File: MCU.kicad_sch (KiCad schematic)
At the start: 21 parts, among them J1 DEBUG, Q1 BC817, Q2 BC817, SW1 RST, U6 ESP32-S3-WROOM-1

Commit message: -add some changes to power section and display
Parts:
- removed J1: DEBUG, Connector_PinHeader_2.54mm:PinHeader_2x06_P2.54mm_Vertical_SMD, symbol Connector_Generic:Conn_02x06_Odd_Even
- removed TP2: P0.29, TestPoint:TestPoint_Pad_D2.0mm, symbol Connector:TestPoint
- added J10: DEBUG, Connector_PinHeader_2.54mm:PinHeader_2x05_P2.54mm_Vertical_SMD, symbol Connector_Generic:Conn_02x05_Odd_Even
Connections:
- net +3.3V: now also J10.2 (Pin_2)
- net DTR: now also J10.9 (Pin_9)
- net GND: now also J10.10 (Pin_10)
- net GPIO_0: now also J10.3 (Pin_3)
- net GPIO_12/JTAG_TDI: now also J10.6 (Pin_6)
- net GPIO_13/JTAG_TCK: now also J10.4 (Pin_4)
- net GPIO_2: now also U6.21 (GPIO13/TOUCH13/ADC2_CH2/FSPIQ/FSPIIO7/SUBSPIQ); no longer U6.38 (GPIO2/TOUCH2/ADC1_CH1)
- net GPIO_25: now also U6.5 (GPIO5/TOUCH5/ADC1_CH4); no longer U6.21 (GPIO13/TOUCH13/ADC2_CH2/FSPIQ/FSPIIO7/SUBSPIQ)
- net GPIO_32: now also U6.39 (GPIO1/TOUCH1/ADC1_CH0); no longer U6.11 (GPIO18/U1RXD/ADC2_CH7/CLK_OUT3)
- net GPIO_33: now also U6.38 (GPIO2/TOUCH2/ADC1_CH1); no longer U6.23 (GPIO21)
- net GPIO_34: now also U6.26 (GPIO45); no longer U6.31 (GPIO38/FSPIWP/SUBSPIWP)
- net GPIO_35: now also U6.16 (GPIO46); no longer U6.26 (GPIO45)
- net GPIO_4: now also U6.11 (GPIO18/U1RXD/ADC2_CH7/CLK_OUT3); no longer U6.4 (GPIO4/TOUCH4/ADC1_CH3)
- net GPIO_5: now also U6.23 (GPIO21); no longer U6.5 (GPIO5/TOUCH5/ADC1_CH4)
- net I2S_DOUT: now also U6.4 (GPIO4/TOUCH4/ADC1_CH3); no longer U6.8 (GPIO15/U0RTS/ADC2_CH4/XTAL_32K_P)
- net RESET: now also J10.1 (Pin_1)
- net RTS: now also J10.8 (Pin_8)
- net SD_SPI_CS: now also U6.31 (GPIO38/FSPIWP/SUBSPIWP); no longer U6.16 (GPIO46)
- net I2C_SCL: now reaches U1.7 (P0.29)
- net I2C_SCL: now also U6.9 (GPIO16/U0CTS/ADC2_CH5/XTAL_32K_N)
- net GPIO_44/RXD0: now reaches U6.36 (U0RXD/GPIO44/CLK_OUT2)
- net GPIO_44/RXD0: now also U1.41 (P0.12), J10.7 (Pin_7)
- net GPIO_43/TXD0: now reaches U6.37 (U0TXD/GPIO43/CLK_OUT1)
- net GPIO_43/TXD0: now also U1.39 (P1.10), J10.5 (Pin_5)
- net I2C_SDA: now reaches U1.23 (P0.01)
- net I2C_SDA: now also U6.8 (GPIO15/U0RTS/ADC2_CH4/XTAL_32K_P)
- removed net GPIO_1/TXD0: U1.41 (P0.12), U6.39 (GPIO1/TOUCH1/ADC1_CH0)
- net GPIO_3/RXD0: no longer names the net of U6.15 (GPIO3/TOUCH3/ADC1_CH2)
- net GPIO_3/RXD0: no longer U1.39 (P1.10)
- no-connect marks 6 -> 3
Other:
- moved on the sheet: C13, C14, FB8, R31, R32, U1

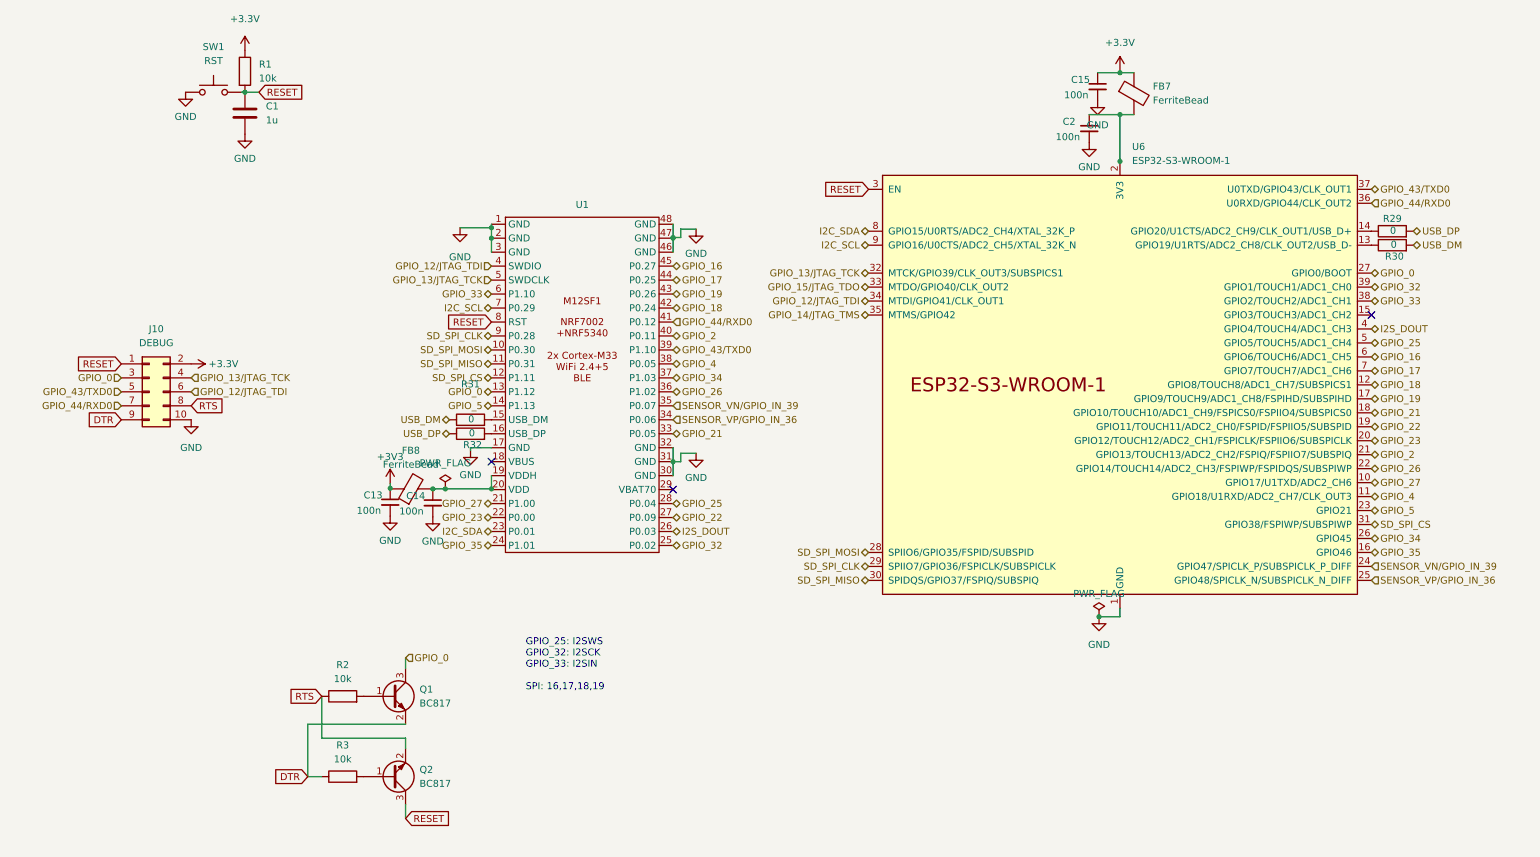
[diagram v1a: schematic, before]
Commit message: -enh repin mcu in schematic
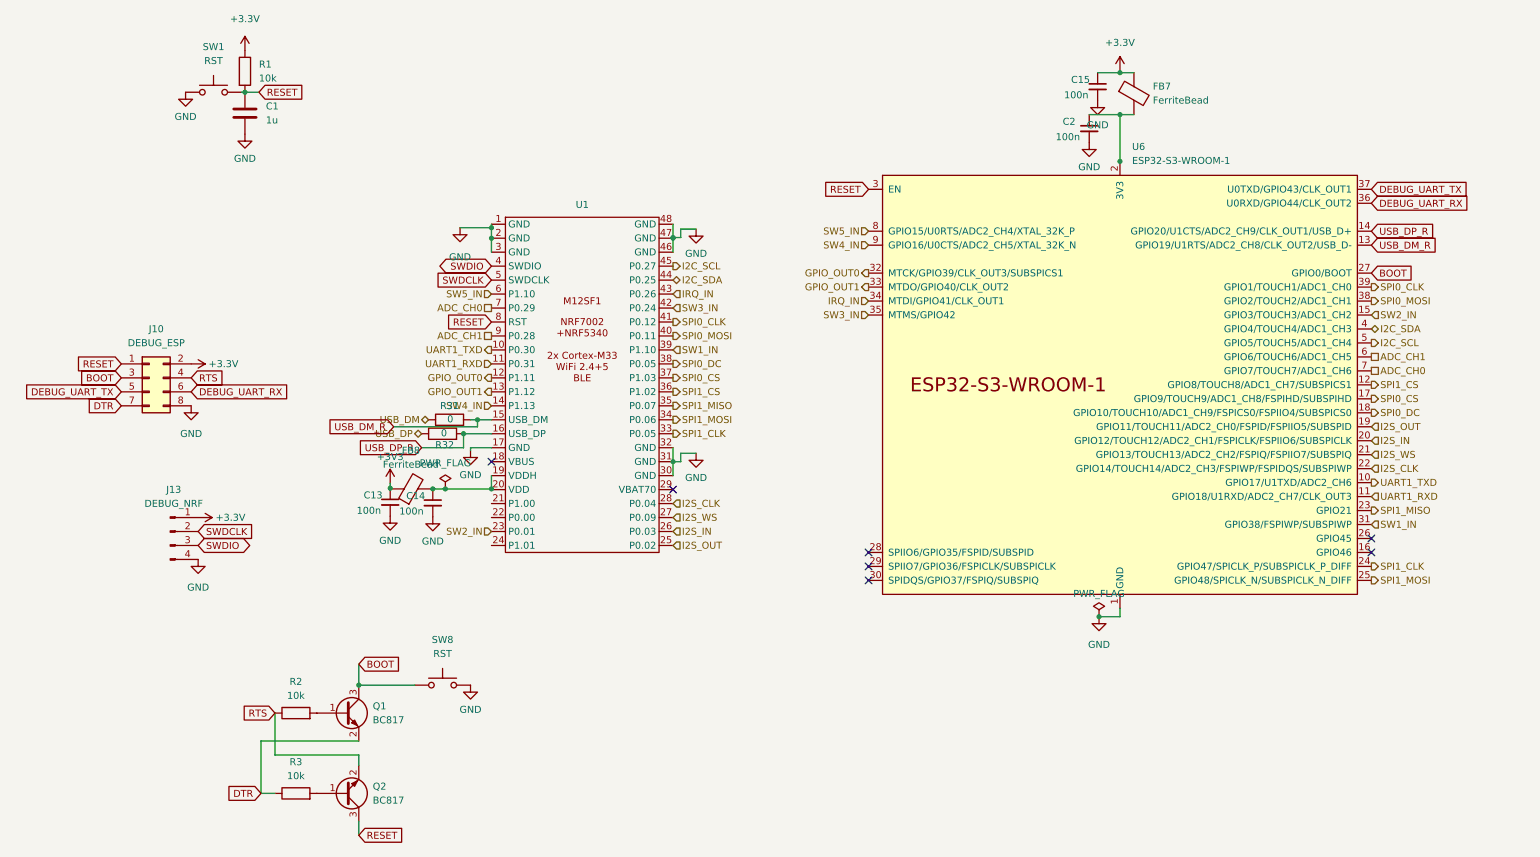
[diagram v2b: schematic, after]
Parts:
- removed J10: DEBUG, Connector_PinHeader_2.54mm:PinHeader_2x05_P2.54mm_Vertical_SMD, symbol Connector_Generic:Conn_02x05_Odd_Even
- removed R29, R30: 0, Resistor_SMD:R_0603_1608Metric_Pad0.98x0.95mm_HandSolder, symbol Device:R
- added J10: DEBUG_ESP, Connector_PinHeader_2.54mm:PinHeader_2x04_P2.54mm_Vertical_SMD, symbol Connector_Generic:Conn_02x04_Odd_Even
- added J13: DEBUG_NRF, Connector_PinHeader_2.54mm:PinHeader_2x02_P2.54mm_Vertical_SMD, symbol Connector:Conn_01x04_Pin
- added SW8: RST, Button_Switch_SMD:SW_SPST_B3S-1000, symbol Switch:SW_Push
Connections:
- net +3.3V: now also J10.2 (Pin_2), J13.1 (Pin_1)
- net DTR: now also J10.7 (Pin_7)
- net GND: now also J10.8 (Pin_8), J13.4 (Pin_4), SW8.2
- net I2C_SCL: now also U1.45 (P0.27), U6.5 (GPIO5/TOUCH5/ADC1_CH4); no longer U1.7 (P0.29), U6.9 (GPIO16/U0CTS/ADC2_CH5/XTAL_32K_N)
- net I2C_SDA: now also U1.44 (P0.25), U6.4 (GPIO4/TOUCH4/ADC1_CH3); no longer U1.23 (P0.01), U6.8 (GPIO15/U0RTS/ADC2_CH4/XTAL_32K_P)
- net RESET: now also J10.1 (Pin_1)
- net RTS: now also J10.4 (Pin_4)
- net USB_DP_R: now reaches U6.14 (GPIO20/U1CTS/ADC2_CH9/CLK_OUT1/USB_D+)
- net USB_DP_R: now also R32.2, U1.16 (USB_DP)
- net USB_DM_R: now reaches U6.13 (GPIO19/U1RTS/ADC2_CH8/CLK_OUT2/USB_D-)
- net USB_DM_R: now also R31.2, U1.15 (USB_DM)
- net SW2_IN: now reaches U6.15 (GPIO3/TOUCH3/ADC1_CH2)
- net SW2_IN: now also U1.23 (P0.01)
- net GPIO_0 renamed BOOT
- net BOOT: now also J10.3 (Pin_3), SW8.1; no longer U1.13 (P1.12)
- net GPIO_12/JTAG_TDI renamed IRQ_IN
- net IRQ_IN: now also U1.43 (P0.26); no longer U1.4 (SWDIO)
- net GPIO_13/JTAG_TCK renamed GPIO_OUT0
- net GPIO_OUT0: now also U1.12 (P1.11); no longer U1.5 (SWDCLK)
- net GPIO_14/JTAG_TMS renamed SW3_IN
- net SW3_IN: now also U1.42 (P0.24)
- net GPIO_15/JTAG_TDO renamed GPIO_OUT1
- net GPIO_OUT1: now also U1.13 (P1.12)
- net GPIO_16 renamed ADC_CH1
- net ADC_CH1: now also U1.9 (P0.28); no longer U1.45 (P0.27)
- net GPIO_17 renamed ADC_CH0
- net ADC_CH0: now also U1.7 (P0.29); no longer U1.44 (P0.25)
- net GPIO_18 renamed SPI1_CS
- net SPI1_CS: now also U1.36 (P1.02); no longer U1.42 (P0.24)
- net GPIO_19 renamed SPI0_CS
- net SPI0_CS: now also U1.37 (P1.03); no longer U1.43 (P0.26)
- net GPIO_2 renamed I2S_WS
- net I2S_WS: now also U1.27 (P0.09); no longer U1.40 (P0.11)
- net GPIO_21 renamed SPI0_DC
- net SPI0_DC: now also U1.38 (P0.05); no longer U1.33 (P0.05)
- net GPIO_22 renamed I2S_OUT
- net I2S_OUT: now also U1.25 (P0.02); no longer U1.27 (P0.09)
- net GPIO_23: no longer names the net of U1.22 (P0.00)
- net GPIO_23: no longer U6.20 (GPIO12/TOUCH12/ADC2_CH1/FSPICLK/FSPIIO6/SUBSPICLK)
- net GPIO_25 renamed I2S_CLK
- net I2S_CLK: now also U6.22 (GPIO14/TOUCH14/ADC2_CH3/FSPIWP/FSPIDQS/SUBSPIWP); no longer U6.5 (GPIO5/TOUCH5/ADC1_CH4)
- removed net GPIO_26: U1.36 (P1.02), U6.22 (GPIO14/TOUCH14/ADC2_CH3/FSPIWP/FSPIDQS/SUBSPIWP)
- net GPIO_27: no longer names the net of U1.21 (P1.00)
- net GPIO_27: no longer U6.10 (GPIO17/U1TXD/ADC2_CH6)
- net GPIO_32 renamed SPI0_CLK
- net SPI0_CLK: now also U1.41 (P0.12); no longer U1.25 (P0.02)
- net GPIO_33 renamed SPI0_MOSI
- net SPI0_MOSI: now also U1.40 (P0.11); no longer U1.6 (P1.10)
- net GPIO_34: no longer names the net of U6.26 (GPIO45)
- net GPIO_34: no longer U1.37 (P1.03)
- net GPIO_35: no longer names the net of U6.16 (GPIO46)
- net GPIO_35: no longer U1.24 (P1.01)
- net GPIO_4 renamed UART1_RXD
- net UART1_RXD: now also U1.11 (P0.31); no longer U1.38 (P0.05)
- net GPIO_43/TXD0 renamed DEBUG_UART_TX
- net DEBUG_UART_TX: now also J10.5 (Pin_5); no longer U1.39 (P1.10)
- net GPIO_44/RXD0 renamed DEBUG_UART_RX
- net DEBUG_UART_RX: now also J10.6 (Pin_6); no longer U1.41 (P0.12)
- net GPIO_5 renamed SPI1_MISO
- net SPI1_MISO: now also U1.35 (P0.07); no longer U1.14 (P1.13)
- net I2S_DOUT renamed I2S_IN
- net I2S_IN: now also U6.20 (GPIO12/TOUCH12/ADC2_CH1/FSPICLK/FSPIIO6/SUBSPICLK); no longer U6.4 (GPIO4/TOUCH4/ADC1_CH3)
- net SD_SPI_CLK: no longer names the net of U6.29 (SPIIO7/GPIO36/FSPICLK/SUBSPICLK)
- net SD_SPI_CLK: no longer U1.9 (P0.28)
- net SD_SPI_CS renamed SW1_IN
- net SW1_IN: now also U1.39 (P1.10); no longer U1.12 (P1.11)
- net SD_SPI_MISO: no longer names the net of U6.30 (SPIDQS/GPIO37/FSPIQ/SUBSPIQ)
- net SD_SPI_MISO: no longer U1.11 (P0.31)
- net SD_SPI_MOSI: no longer names the net of U6.28 (SPIIO6/GPIO35/FSPID/SUBSPID)
- net SD_SPI_MOSI: no longer U1.10 (P0.30)
- net SENSOR_VN/GPIO_IN_39 renamed SPI1_CLK
- net SPI1_CLK: now also U1.33 (P0.05); no longer U1.35 (P0.07)
- net SENSOR_VP/GPIO_IN_36 renamed SPI1_MOSI
- new net SW4_IN: U1.14 (P1.13), U6.9 (GPIO16/U0CTS/ADC2_CH5/XTAL_32K_N)
- new net SW5_IN: U1.6 (P1.10), U6.8 (GPIO15/U0RTS/ADC2_CH4/XTAL_32K_P)
- new net SWDCLK: J13.2 (Pin_2), U1.5 (SWDCLK)
- new net SWDIO: J13.3 (Pin_3), U1.4 (SWDIO)
- new net UART1_TXD: U1.10 (P0.30), U6.10 (GPIO17/U1TXD/ADC2_CH6)
- no-connect marks 3 -> 7
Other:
- note removed: "GPIO_25: I2SWS GPIO_32: I2SCK GPIO_33: I2SIN SPI: 16,17,18,19"
- moved on the sheet: Q1, Q2, R2, R3, R31, R32

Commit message: -add soft latching circuit, routing mostly done
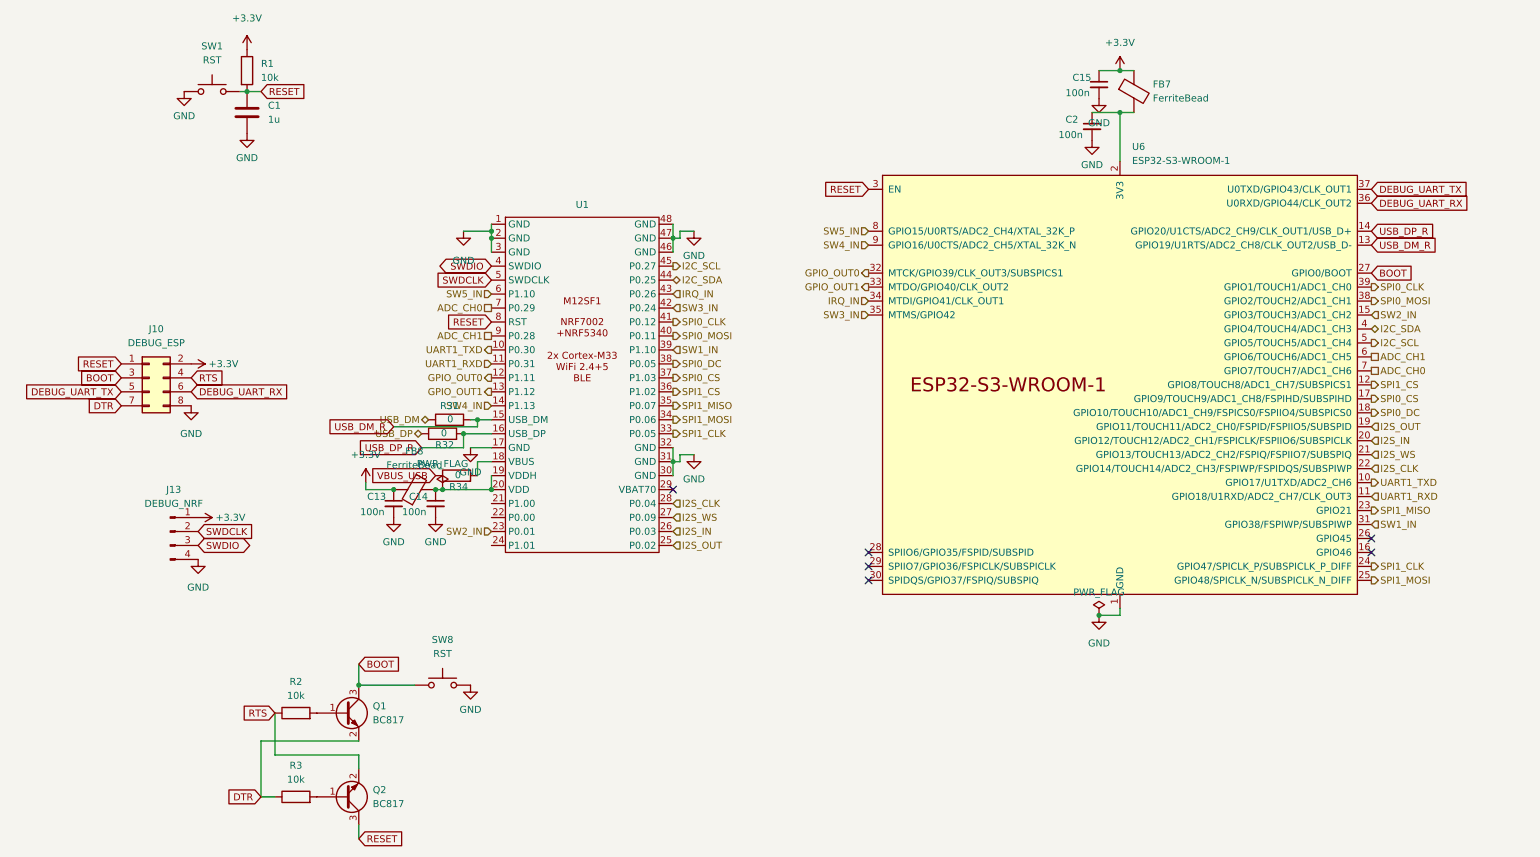
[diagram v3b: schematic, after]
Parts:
- added R34: 0, Resistor_SMD:R_0603_1608Metric_Pad0.98x0.95mm_HandSolder, symbol Device:R
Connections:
- net +3V3 is gone; now on net +3.3V: C13.1, FB8.1
- net at U1.18 (VBUS): now also R34.2
- new net VBUS_USB: R34.1
- no-connect marks 7 -> 6
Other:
- moved on the sheet: C13, C14, C2, FB8, Q2, R3

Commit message: -add end revision
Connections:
- net SW2_IN: now also U6.35 (MTMS/GPIO42); no longer U6.15 (GPIO3/TOUCH3/ADC1_CH2)
- net SW3_IN: now also U1.22 (P0.00), U6.16 (GPIO46); no longer U1.42 (P0.24), U6.35 (MTMS/GPIO42)
- new net SPI0_MISO: U1.42 (P0.24), U6.15 (GPIO3/TOUCH3/ADC1_CH2)
- no-connect marks 6 -> 5
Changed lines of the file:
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@@
-	)
-	(no_connect
-		(at 261.62 118.11)
 	)
 	(no_connect
@@
 		)
 	)
-	(hierarchical_label "SW2_IN"
-		(shape input)
-		(at 261.62 74.93 0)
-		(fields_autoplaced yes)
-		(effects
-			(font
-				(size 1.27 1.27)
-			)
-			(justify left)
-		)
-	)
 	(hierarchical_label "SPI0_MOSI"
 		(shape output)
@@
 		)
 	)
+	(hierarchical_label "SW3_IN"
+		(shape input)
+		(at 101.6 111.76 180)
+		(fields_autoplaced yes)
+		(effects
+			(font
+				(size 1.27 1.27)
+			)
+			(justify right)
+		)
+	)
 	(hierarchical_label "SPI1_CLK"
 		(shape output)
@@
 		)
 	)
-	(hierarchical_label "SW3_IN"
-		(shape input)
-		(at 134.62 73.66 0)
-		(fields_autoplaced yes)
-		(effects
-			(font
-				(size 1.27 1.27)
-			)
-			(justify left)
-		)
-	)
 	(hierarchical_label "SW5_IN"
 		(shape input)
@@
 		)
 	)
+	(hierarchical_label "SW2_IN"
+		(shape input)
+		(at 170.18 74.93 180)
+		(fields_autoplaced yes)
+		(effects
+			(font
+				(size 1.27 1.27)
+			)
+			(justify right)
+		)
+	)
 	(hierarchical_label "I2C_SCL"
 		(shape output)
@@
 		)
 	)
+	(hierarchical_label "SW3_IN"
+		(shape input)
+		(at 261.62 118.11 0)
+		(fields_autoplaced yes)
+		(effects
+			(font
+				(size 1.27 1.27)
+			)
+			(justify left)
+		)
+	)
 	(hierarchical_label "SPI1_CS"
 		(shape output)
@@
 		)
 	)
+	(hierarchical_label "SPI0_MISO"
+		(shape input)
+		(at 134.62 73.66 0)
+		(fields_autoplaced yes)
+		(effects
+			(font
+				(size 1.27 1.27)
+			)
+			(justify left)
+		)
+	)
 	(hierarchical_label "I2S_IN"
 		(shape input)
@@
 		(shape output)
 		(at 101.6 88.9 180)
-		(fields_autoplaced yes)
-		(effects
-			(font
-				(size 1.27 1.27)
-			)
-			(justify right)
-		)
-	)
-	(hierarchical_label "SW3_IN"
-		(shape input)
-		(at 170.18 74.93 180)
 		(fields_autoplaced yes)
 		(effects
@@
 		)
 	)
+	(hierarchical_label "SPI0_MISO"
+		(shape input)
+		(at 261.62 74.93 0)
+		(fields_autoplaced yes)
+		(effects
+			(font
+				(size 1.27 1.27)
+			)
+			(justify left)
+		)
+	)
